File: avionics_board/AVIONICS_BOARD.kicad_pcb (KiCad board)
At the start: 4 copper layers, 80 x 80 mm, 156 parts, among them J1 Conn_02x03_Odd_Even, J10 Conn_02x03_Odd_Even, J11 Conn_02x03_Odd_Even, J12 Conn_02x03_Odd_Even, J13 Conn_02x03_Odd_Even, J14 Conn_02x05_Odd_Even, J15 Conn_02x05_Odd_Even, J2 Conn_02x03_Odd_Even, J3 Conn_02x03_Odd_Even, J4 Conn_02x03_Odd_Even, J5 Conn_01x06, J6 Conn_01x04, J7 PC104 Conn_02x20_Odd_Even, J8 Conn_02x04, J9 10155435-00011LF, SW1 EVP-AA602W, SW2 SW_DIP_x01, SW3 EVP-AA602W, U1 STM32L496ZGTx, U10 TCAN3414, U11 TCAN3414, U12 74LVC2G07, U13 INA226, U14 DRV8838, U15 TCA9548APWR, U16 AP3602AKTR-G1, U2 MMC5983MA, U3 BMI270, U4 INA226, U5 DRV8838, U6 TPL5010, U7 INA226, U8 DRV8838, U9 MR25H10, X1 10MHz, X2 32.768KHZ

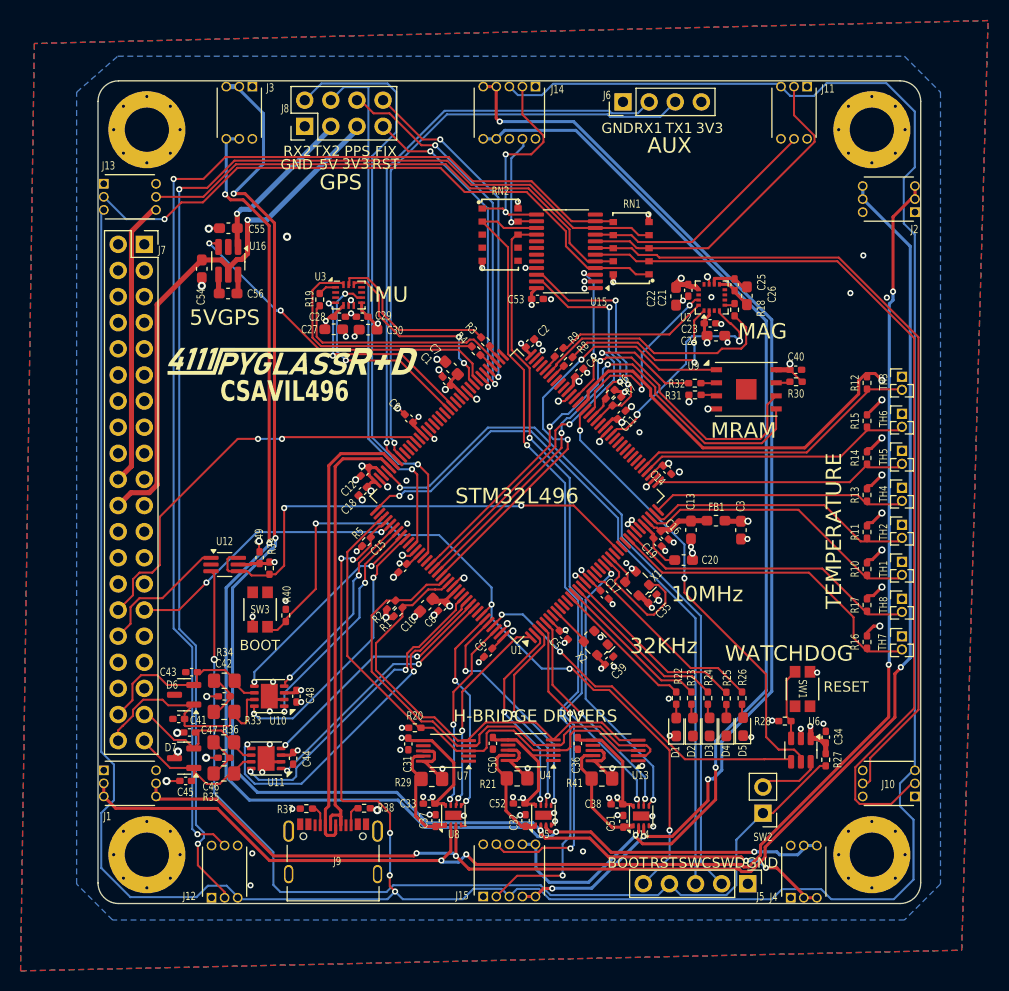
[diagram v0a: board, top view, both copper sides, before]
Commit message: add SPI CS and MISO pullups and terminations, remove WD from SCI
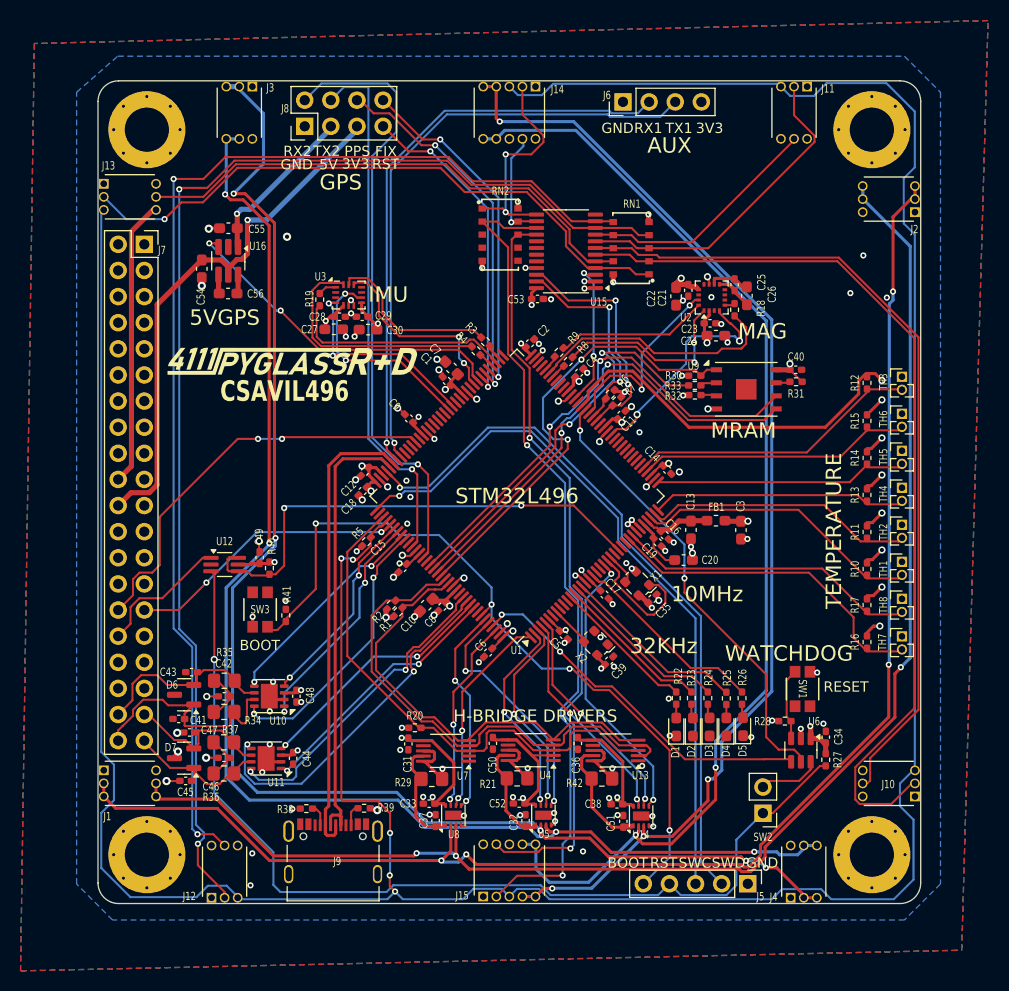
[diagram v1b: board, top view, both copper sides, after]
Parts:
- added R30: 100K, Resistor_SMD:R_0402_1005Metric_Pad0.72x0.64mm_HandSolder, F.Cu at (118.0, 88.7)
- moved R33 0.22 mm to (118.0, 89.6)
- renumbered R30 to R31, R31 to R32, R32 to R33, R33 to R34, R34 to R35, R35 to R36, R36 to R37, R37 to R38, R38 to R39, R39 to R40, R40 to R41, R41 to R42
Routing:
- net /STM32L4/SPI3_SCK: track 51.2 -> 47.4 mm
- net /STM32L4/SPI3_MOSI: track 49.6 -> 46.2 mm
- net /TEMP_PWR: track 74.8 -> 72.7 mm
- net /3.3V_MRAM: track 106.4 -> 107.5 mm, vias 2 -> 3

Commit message: QC, add second 3V regulator to AUX, INT pullups on AUX SCI AVI
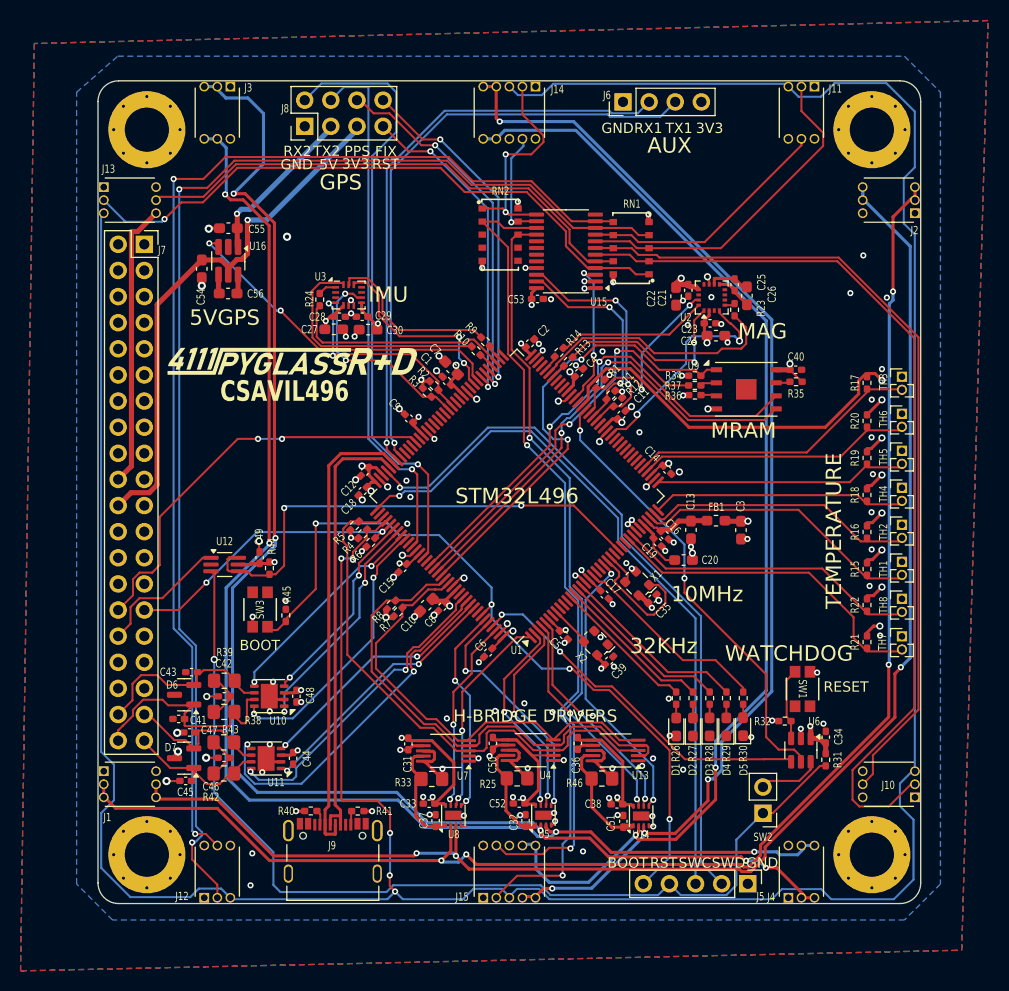
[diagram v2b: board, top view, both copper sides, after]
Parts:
- removed the R20 at (90.8, 122.9)
- removed the R22 at (116.2, 120.0)
- removed the R23 at (117.7, 120.0)
- removed the R24 at (119.3, 120.0)
- removed the R25 at (121.1, 120.0)
- removed the R38 at (80.3, 130.8)
- removed the R39 at (85.9, 130.7)
- added R1: 100K, Resistor_SMD:R_0402_1005Metric_Pad0.72x0.64mm_HandSolder, F.Cu at (108.8, 89.5)
- added R2: 100K, Resistor_SMD:R_0402_1005Metric_Pad0.72x0.64mm_HandSolder, F.Cu at (92.7, 89.6)
- added R27: 1K, Resistor_SMD:R_0402_1005Metric_Pad0.72x0.64mm_HandSolder, F.Cu at (117.8, 120.0)
- added R28: 1K, Resistor_SMD:R_0402_1005Metric_Pad0.72x0.64mm_HandSolder, F.Cu at (119.5, 120.0)
- added R29: 1K, Resistor_SMD:R_0402_1005Metric_Pad0.72x0.64mm_HandSolder, F.Cu at (121.1, 120.0)
- added R3: 100K, Resistor_SMD:R_0402_1005Metric_Pad0.72x0.64mm_HandSolder, F.Cu at (92.0, 90.3)
- added R30: 1K, Resistor_SMD:R_0402_1005Metric_Pad0.72x0.64mm_HandSolder, F.Cu at (122.7, 120.0)
- added R4: 100K, Resistor_SMD:R_0402_1005Metric_Pad0.72x0.64mm_HandSolder, F.Cu at (85.7, 104.0)
- added R40: 5K1, Resistor_SMD:R_0402_1005Metric_Pad0.72x0.64mm_HandSolder, F.Cu at (80.7, 131.0)
- added R41: 5K1, Resistor_SMD:R_0402_1005Metric_Pad0.72x0.64mm_HandSolder, F.Cu at (85.3, 131.0)
- added R6: 300K, Resistor_SMD:R_0402_1005Metric_Pad0.72x0.64mm_HandSolder, F.Cu at (86.5, 104.9)
- C13, C20, C27, C3, C30: value 1uF -> 10u
- J9: footprint Common:AMPHENOL_10155435-00011LF -> Project:AMPHENOL_10155435-00011LF
- SW3: footprint Project:EVP602AA -> Common:EVP602AA
- moved R26 6.41 mm to (116.2, 120.0), turned to -90 degrees
- moved J3 2.14 mm to (71.6, 63.1)
- moved R5 1.94 mm to (84.9, 103.3)
- moved J11 0.72 mm to (128.4, 63.1)
- moved J12 0.71 mm to (71.6, 136.9)
- moved J13 0.32 mm to (63.1, 71.6)
- moved J4 0.23 mm to (128.4, 136.9)
- moved R12 0.12 mm to (110.5, 91.2)
- moved J15 0.12 mm to (100.0, 136.9)
- moved J2 0.10 mm to (136.9, 71.6)
- moved R11 0.10 mm to (109.9, 90.5)
- moved J1 0.09 mm to (63.1, 128.4)
- moved J10 0.08 mm to (136.9, 128.4)
- moved J9 0.06 mm to (82.8, 137.1)
- renumbered R4 to R10, R6 to R11, R7 to R12, R8 to R13, R9 to R14, R10 to R15, R11 to R16, R12 to R17, R13 to R18, R14 to R19, R15 to R20, R16 to R21, R17 to R22, R18 to R23, R19 to R24, R21 to R25, R27 to R31, R28 to R32, R29 to R33, R30 to R34, R31 to R35, R32 to R36, R33 to R37, R34 to R38, R35 to R39, R36 to R42, R37 to R43, R40 to R44, R41 to R45, R42 to R46, R1 to R7, R2 to R8, R3 to R9
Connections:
- net /GYRO_INT_1 renamed /GYRO1_INT
- net /GYRO_INT_2 renamed /GYRO2_INT
- net /STM32L4/USB/USB_OTG_FS_DM renamed /STM32L4/USB/DN
- net /STM32L4/USB/USB_OTG_FS_DP renamed /STM32L4/USB/DP
- net /STM32L4/USB/VUSB1 renamed /STM32L4/USB/VBUS1
- net /STM32L4/USB/VUSB2 renamed /STM32L4/USB/VBUS2
- R26 pad 1: Net-(D5-A) -> /STM32L4/LED_1
- R26 pad 2: /STM32L4/LED_5 -> Net-(D1-A)
- R5 pad 2: /SUN_INT -> /ACS_INT
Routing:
- net GND: track 54.2 -> 61.9 mm, vias 98 -> 118
- net /3.3V_STM_CORE: track 53.1 -> 56.9 mm, vias 24 -> 27
- net /ACS/Y_P: track 136.2 -> 138.3 mm
- net /STM32L4/SPI3_MISO: track 39.0 -> 37.3 mm
- net /ACS_INT: track 51.8 -> 53.5 mm
- net /Solar Sensors/SD2: track 32.1 -> 33.2 mm
- net /Solar Sensors/SC2: track 23.7 -> 24.8 mm
- net /*ATTENTION: track 27.4 -> 28.3 mm
- net /3.3V_SUN: track 307.3 -> 308.0 mm
- net /ACS/X_N: track 140.7 -> 140.0 mm
- net /3.3V_ACS_LOGIC: track 94.7 -> 94.0 mm, vias 5 -> 4
- net /STM32L4/MRAM_CS: track 44.5 -> 45.1 mm
- net /Solar Sensors/SD3: track 120.6 -> 121.2 mm
- net /Solar Sensors/SC3: track 113.9 -> 113.3 mm
- net /Solar Sensors/SD1: track 88.2 -> 88.8 mm
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
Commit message: propate the changes to RF
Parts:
- R6: value 300K -> 330K
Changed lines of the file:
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@@
 			)
 		)
-		(property "Value" "300K"
+		(property "Value" "330K"
 			(at 0 1.17 45)
 			(layer "F.Fab")
@@
 			)
 		)
-		(property "Part Number" "RC0402FR-07300KL"
+		(property "Part Number" "RC0402FR-07330KL"
 			(at 0 0 45)
 			(unlocked yes)

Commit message: tweaks before merge
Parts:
- J9: footprint Project:AMPHENOL_10155435-00011LF -> Common:AMPHENOL_10155435-00011LF
